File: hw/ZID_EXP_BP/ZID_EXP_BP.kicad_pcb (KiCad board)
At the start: 4 copper layers, 127 x 101.6 mm, 65 parts, among them J1 FFC/FPC-40 Socket, J15 JST-PH-K B6B, J2 Conn 2x04 0.1" pin, J3 Conn 2x02 0.1" pin, J4 Conn 2x04 0.1" pin, Q1 DMG2305UX, SW1 SW_DIP_x08, U1 ATF1502AS-44T

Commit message: PCB: Ready to order - ZID, POD1, POD2, POD3, POD4, ExpBP
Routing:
- net GND: track 91.4 -> 111.6 mm, vias 110 -> 112
- net /D2: track 165.7 -> 166.9 mm

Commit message: PCB: ExpBP, add power LED
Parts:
- added LED1: LED BLUE, LED_SMD:LED_0805_2012Metric, F.Cu at (193.2, 46.2)
- added R17: 1.2k, Resistor_SMD:R_0805_2012Metric, F.Cu at (192.9, 49.9)
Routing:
- net +5V: track 109.8 -> 113.8 mm, vias 24 -> 25
- net GND: track 111.6 -> 115.2 mm
- net Net-(LED1-K): track 0.00 -> 1.92 mm

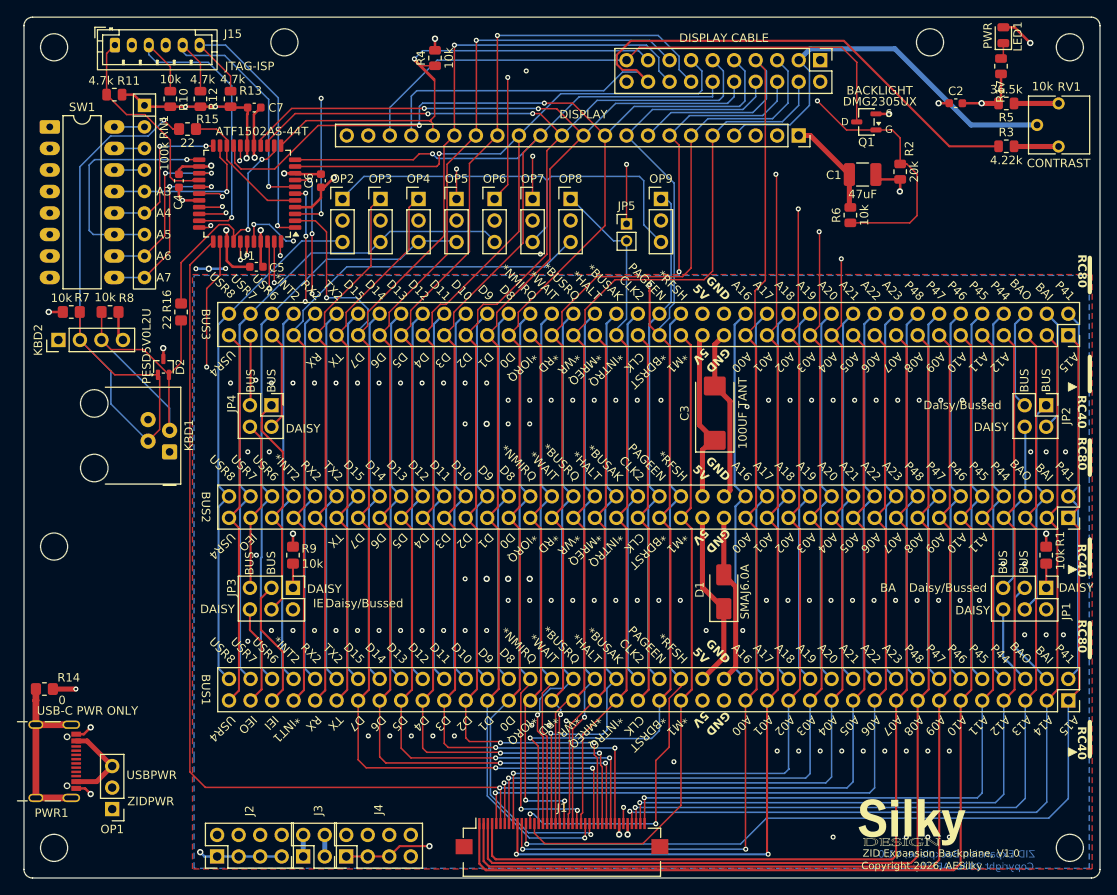
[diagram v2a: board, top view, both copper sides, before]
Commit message: PCB: Change all SMD resistors to the same package.
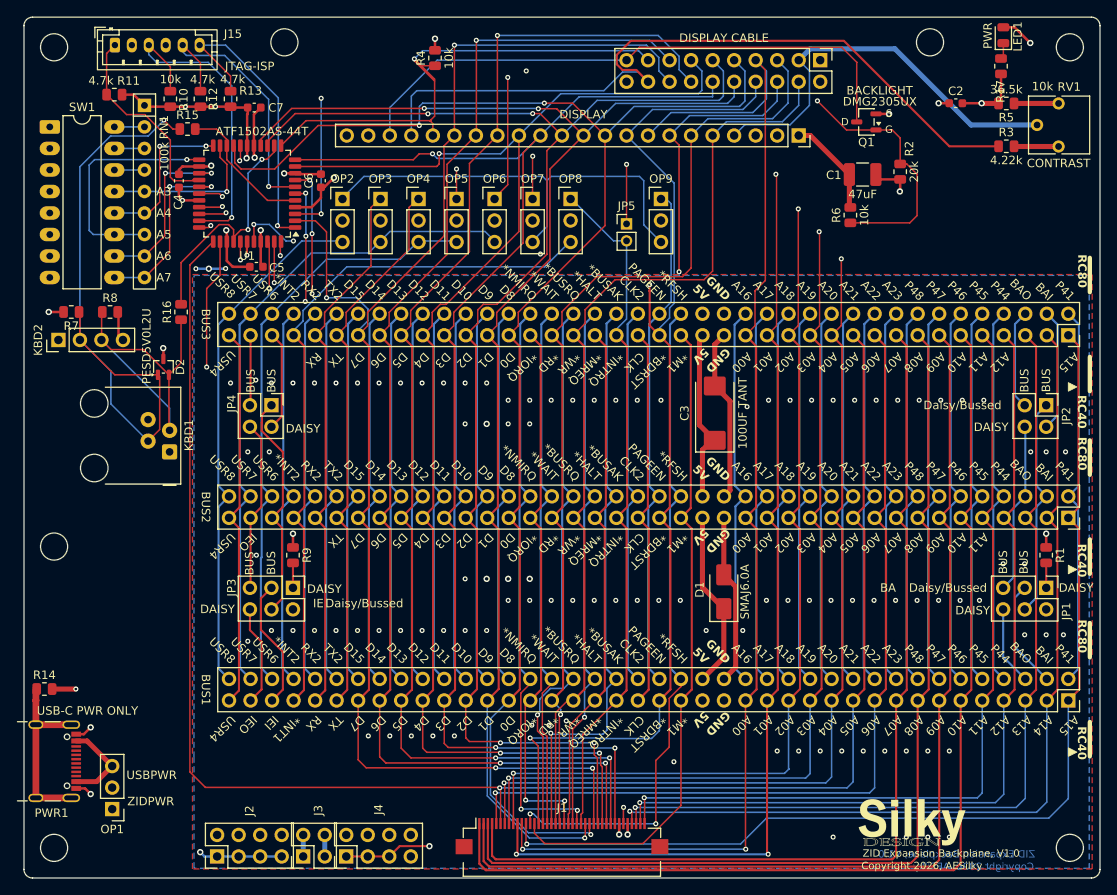
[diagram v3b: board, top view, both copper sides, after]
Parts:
- R1, R14, R15, R16, R7, R8, R9: footprint Resistor_SMD:R_0805_2012Metric_Pad1.20x1.40mm_HandSolder -> Resistor_SMD:R_0805_2012Metric
